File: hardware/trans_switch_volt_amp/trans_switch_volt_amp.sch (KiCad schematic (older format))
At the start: 19 parts, among them J1 to biopac, J2 To biopac, Q1 BC182L_NPN, Q2 BC182L_NPN, U1 LM741, U2 LM741

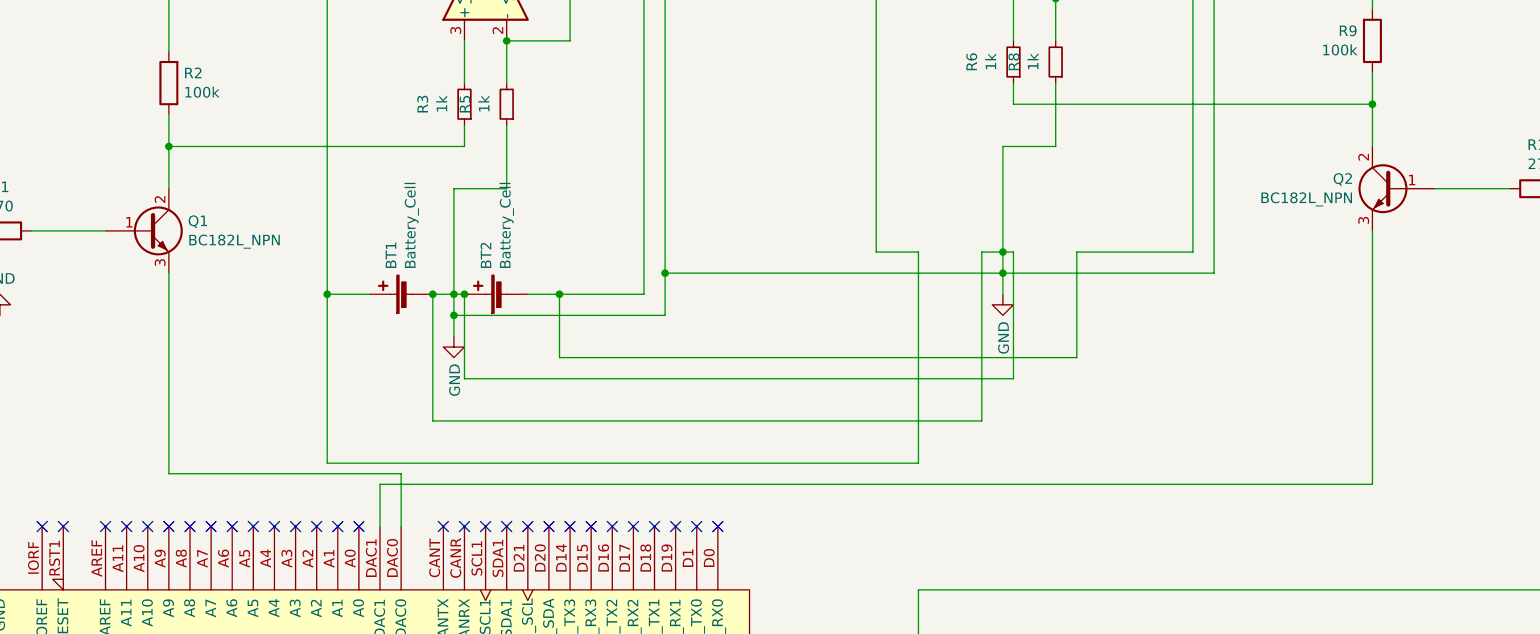
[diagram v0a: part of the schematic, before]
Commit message: update board and fixed transistor bug
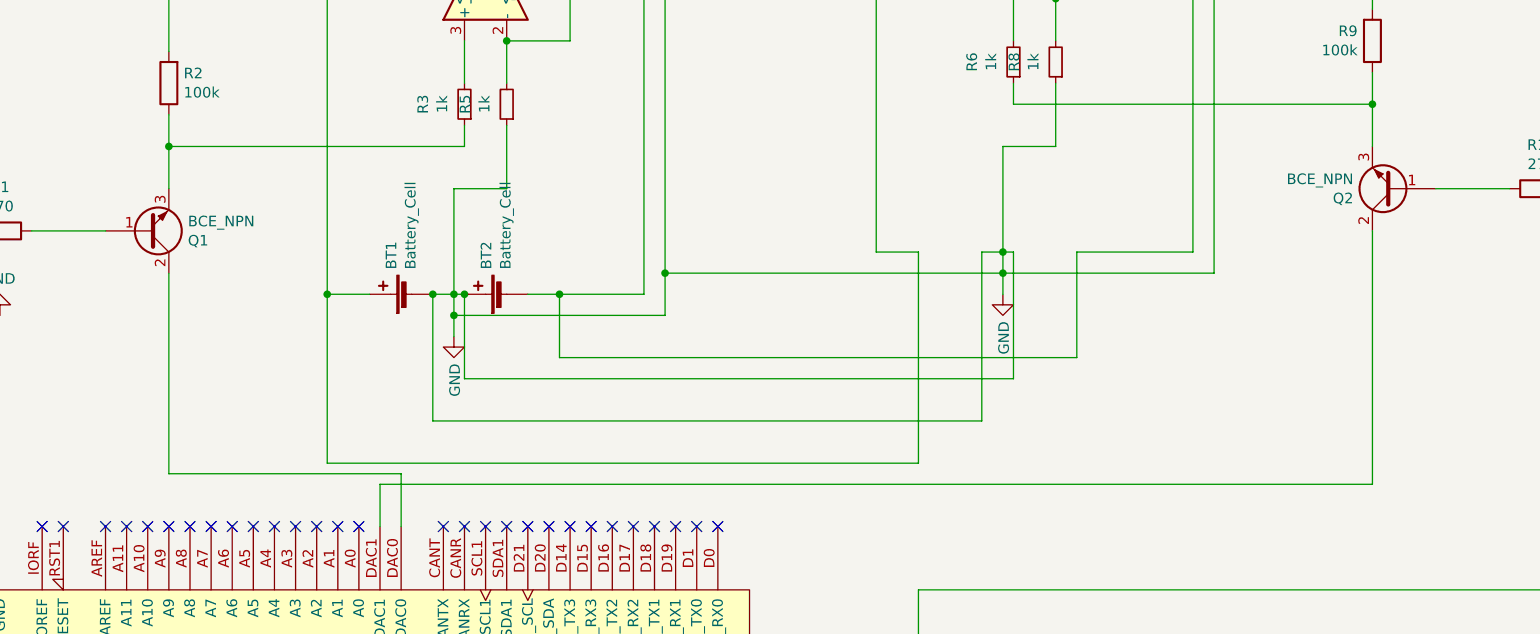
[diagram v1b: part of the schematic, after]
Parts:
- Q1, Q2: value BC182L_NPN -> BCE_NPN
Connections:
- net at R2.1, R3.1: now also Q1.3 (E); no longer Q1.2 (C)
- net at XA1.DAC0: now also Q1.2 (C); no longer Q1.3 (E)
- net at R6.1, R9.1: now also Q2.3 (E); no longer Q2.2 (C)
- net at XA1.DAC1: now also Q2.2 (C); no longer Q2.3 (E)
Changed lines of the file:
@@
 P 8900 3350
 F 0 "Q2" H 9090 3396 50  0000 L CNN
-F 1 "BC182L_NPN" H 9090 3305 50  0000 L CNN
+F 1 "BCE_NPN" H 9090 3305 50  0000 L CNN
 F 2 "Package_TO_SOT_THT:TO-92L_Wide" H 9100 3450 50  0001 C CNN
 F 3 "~" H 8900 3350 50  0001 C CNN
 	1    8900 3350
-	-1   0    0    -1
+	-1   0    0    1
 $EndComp
 $Comp
@@
 	3850 3850 3850 2450
 $Comp
-L Device:Q_NPN_BCE Q1
-U 1 1 5D8A091B
-P 3000 3550
-F 0 "Q1" H 3190 3596 50  0000 L CNN
-F 1 "BC182L_NPN" H 3190 3505 50  0000 L CNN
-F 2 "Package_TO_SOT_THT:TO-92L_Wide" H 3200 3650 50  0001 C CNN
-F 3 "~" H 3000 3550 50  0001 C CNN
-	1    3000 3550
-	1    0    0    -1
-$EndComp
-$Comp
 L Device:R R1
 U 1 1 5D8A39C8
@@
 	3100 2450 3100 2700
 Wire Wire Line
-	3100 3350 3100 3150
-Wire Wire Line
 	4500 3150 3100 3150
-Connection ~ 3100 3150
 Wire Wire Line
 	3100 3150 3100 3000
 Wire Wire Line
-	8800 2800 8800 2950
-Wire Wire Line
 	8800 2950 7100 2950
-Connection ~ 8800 2950
-Wire Wire Line
-	8800 2950 8800 3150
 Wire Wire Line
 	5450 3750 7050 3750
@@
 	4100 4750 8800 4750
 Wire Wire Line
-	8800 3550 8800 4750
-Wire Wire Line
 	4200 4950 4200 4700
 Wire Wire Line
 	4200 4700 3100 4700
-Wire Wire Line
-	3100 3750 3100 4700
 NoConn ~ 5000 7550
 Wire Wire Line
@@
 Wire Wire Line
 	2300 3950 2300 4950
+$Comp
+L Device:Q_NPN_BCE Q1
+U 1 1 5D8A091B
+P 3000 3550
+F 0 "Q1" H 3190 3596 50  0000 L CNN
+F 1 "BCE_NPN" H 3190 3505 50  0000 L CNN
+F 2 "Package_TO_SOT_THT:TO-92L_Wide" H 3200 3650 50  0001 C CNN
+F 3 "~" H 3000 3550 50  0001 C CNN
+	1    3000 3550
+	1    0    0    1
+$EndComp
+Wire Wire Line
+	3100 4700 3100 3750
+Wire Wire Line
+	3100 3350 3100 3150
+Connection ~ 3100 3150
+Wire Wire Line
+	8800 4750 8800 3550
+Wire Wire Line
+	8800 2800 8800 2950
+Connection ~ 8800 2950
+Wire Wire Line
+	8800 2950 8800 3150
 $EndSCHEMATC
